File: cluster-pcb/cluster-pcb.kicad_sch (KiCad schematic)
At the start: 0 parts

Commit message: Progress toward v2.0
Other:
- sheet microcontroller ports: added none; removed ENABLE_TXRX_0, ENABLE_TXRX_1, ENABLE_TXRX_2, ENABLE_TXRX_3, ENABLE_TXRX_4, ENABLE_TXRX_5, ENABLE_TXRX_6, MUX_ADDRESS_0, MUX_ADDRESS_1, MUX_ADDRESS_2, RX, TX
- sheet prism-0 ports: added CIPO, COPI, SCK, ~{CS}; removed none
- sheet prism-1 ports: added CIPO, COPI, SCK, ~{CS}; removed none
- sheet prism-2 ports: added CIPO, COPI, SCK, ~{CS}; removed none
- sheet prism-3 ports: added CIPO, COPI, SCK, ~{CS}; removed ENABLE_TXRX, RX, TX
- sheet prism-4 ports: added CIPO, COPI, SCK, ~{CS}; removed none
- sheet prism-5 ports: added CIPO, COPI, SCK, ~{CS}; removed none
- sheet prism-6 ports: added CIPO, COPI, SCK, ~{CS}; removed none

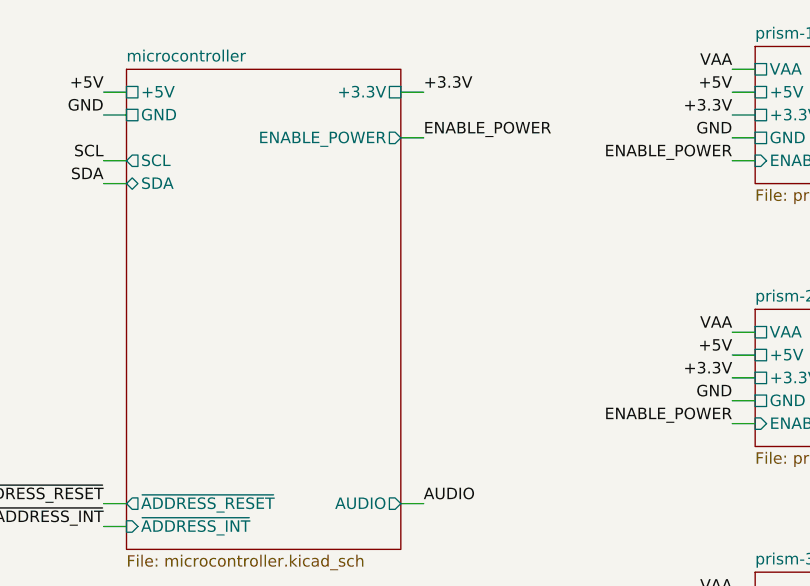
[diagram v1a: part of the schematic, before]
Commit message: Initial pcb layout
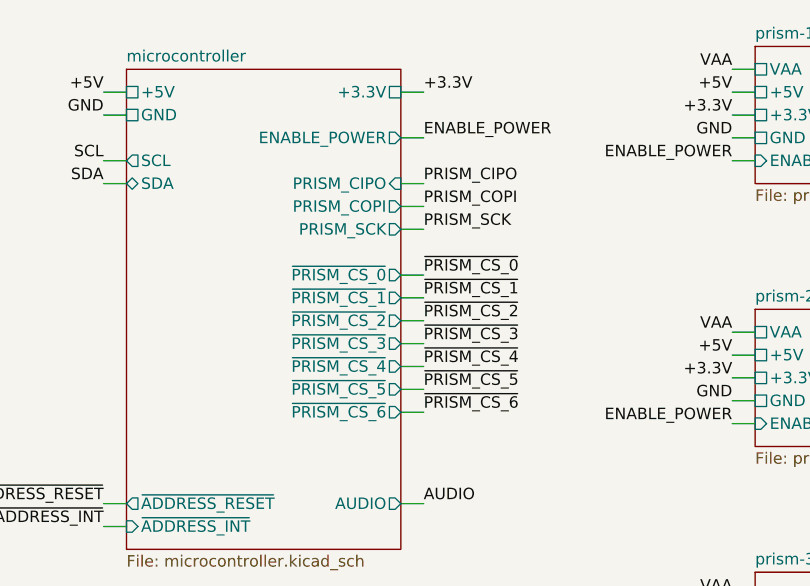
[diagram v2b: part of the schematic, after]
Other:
- sheet microcontroller ports: added PRISM_CIPO, PRISM_COPI, PRISM_SCK, ~{PRISM_CS_0}, ~{PRISM_CS_1}, ~{PRISM_CS_2}, ~{PRISM_CS_3}, ~{PRISM_CS_4}, ~{PRISM_CS_5}, ~{PRISM_CS_6}; removed none
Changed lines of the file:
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@@
   (title_block
     (title "cluster-pcb")
-    (date "2024-09-20")
+    (date "2024-09-27")
     (rev "2.0")
     (company "Howard Hughes Medical Institute")
   )
+  (wire (pts (xy 120.65 78.74) (xy 123.19 78.74))
+    (stroke (width 0) (type default))
+  )
+  (wire (pts (xy 120.65 88.9) (xy 123.19 88.9))
+    (stroke (width 0) (type default))
+  )
   (wire (pts (xy 242.57 41.91) (xy 245.11 41.91))
     (stroke (width 0) (type default))
   )
+  (wire (pts (xy 120.65 101.6) (xy 123.19 101.6))
+    (stroke (width 0) (type default))
+  )
   (wire (pts (xy 177.8 34.29) (xy 180.34 34.29))
     (stroke (width 0) (type default))
   )
+  (wire (pts (xy 120.65 99.06) (xy 123.19 99.06))
+    (stroke (width 0) (type default))
+  )
   (wire (pts (xy 177.8 39.37) (xy 180.34 39.37))
     (stroke (width 0) (type default))
@@
     (stroke (width 0) (type default))
   )
+  (wire (pts (xy 120.65 91.44) (xy 123.19 91.44))
+    (stroke (width 0) (type default))
+  )
   (wire (pts (xy 87.63 66.04) (xy 90.17 66.04))
     (stroke (width 0) (type default))
@@
     (stroke (width 0) (type default))
   )
+  (wire (pts (xy 120.65 86.36) (xy 123.19 86.36))
+    (stroke (width 0) (type default))
+  )
   (wire (pts (xy 222.25 34.29) (xy 224.79 34.29))
     (stroke (width 0) (type default))
@@
     (stroke (width 0) (type default))
   )
+  (wire (pts (xy 120.65 81.28) (xy 123.19 81.28))
+    (stroke (width 0) (type default))
+  )
   (wire (pts (xy 123.19 66.04) (xy 120.65 66.04))
     (stroke (width 0) (type default))
@@
     (stroke (width 0) (type default))
   )
+  (wire (pts (xy 120.65 93.98) (xy 123.19 93.98))
+    (stroke (width 0) (type default))
+  )
   (wire (pts (xy 120.65 71.12) (xy 123.19 71.12))
     (stroke (width 0) (type default))
@@
     (stroke (width 0) (type default))
   )
+  (wire (pts (xy 120.65 96.52) (xy 123.19 96.52))
+    (stroke (width 0) (type default))
+  )
   (wire (pts (xy 160.02 44.45) (xy 157.48 44.45))
     (stroke (width 0) (type default))
@@
     (stroke (width 0) (type default))
   )
+  (wire (pts (xy 120.65 76.2) (xy 123.19 76.2))
+    (stroke (width 0) (type default))
+  )
   (wire (pts (xy 222.25 97.79) (xy 224.79 97.79))
     (stroke (width 0) (type default))
@@
     (effects (font (size 1.27 1.27)) (justify left bottom))
   )
+  (label "~{PRISM_CS_4}" (at 123.19 96.52 0) (fields_autoplaced)
+    (effects (font (size 1.27 1.27)) (justify left bottom))
+  )
   (label "AUDIO" (at 123.19 111.76 0) (fields_autoplaced)
     (effects (font (size 1.27 1.27)) (justify left bottom))
@@
     (effects (font (size 1.27 1.27)) (justify right bottom))
   )
+  (label "PRISM_CIPO" (at 123.19 76.2 0) (fields_autoplaced)
+    (effects (font (size 1.27 1.27)) (justify left bottom))
+  )
   (label "PRISM_COPI" (at 245.11 95.25 0) (fields_autoplaced)
     (effects (font (size 1.27 1.27)) (justify left bottom))
@@
     (effects (font (size 1.27 1.27)) (justify right bottom))
   )
+  (label "~{PRISM_CS_6}" (at 123.19 101.6 0) (fields_autoplaced)
+    (effects (font (size 1.27 1.27)) (justify left bottom))
+  )
   (label "PRISM_CIPO" (at 180.34 92.71 0) (fields_autoplaced)
     (effects (font (size 1.27 1.27)) (justify left bottom))
   )
+  (label "~{PRISM_CS_1}" (at 123.19 88.9 0) (fields_autoplaced)
+    (effects (font (size 1.27 1.27)) (justify left bottom))
+  )
   (label "GND" (at 157.48 41.91 180) (fields_autoplaced)
     (effects (font (size 1.27 1.27)) (justify right bottom))
@@
     (effects (font (size 1.27 1.27)) (justify right bottom))
   )
+  (label "~{PRISM_CS_3}" (at 123.19 93.98 0) (fields_autoplaced)
+    (effects (font (size 1.27 1.27)) (justify left bottom))
+  )
   (label "+3.3V" (at 222.25 68.58 180) (fields_autoplaced)
     (effects (font (size 1.27 1.27)) (justify right bottom))
@@
     (effects (font (size 1.27 1.27)) (justify left bottom))
   )
+  (label "PRISM_SCK" (at 123.19 81.28 0) (fields_autoplaced)
+    (effects (font (size 1.27 1.27)) (justify left bottom))
+  )
   (label "PRISM_SCK" (at 245.11 68.58 0) (fields_autoplaced)
     (effects (font (size 1.27 1.27)) (justify left bottom))
@@
     (effects (font (size 1.27 1.27)) (justify right bottom))
   )
+  (label "~{PRISM_CS_5}" (at 123.19 99.06 0) (fields_autoplaced)
+    (effects (font (size 1.27 1.27)) (justify left bottom))
+  )
   (label "+3.3V" (at 157.48 97.79 180) (fields_autoplaced)
     (effects (font (size 1.27 1.27)) (justify right bottom))
@@
     (effects (font (size 1.27 1.27)) (justify left bottom))
   )
+  (label "~{PRISM_CS_2}" (at 123.19 91.44 0) (fields_autoplaced)
+    (effects (font (size 1.27 1.27)) (justify left bottom))
+  )
+  (label "PRISM_COPI" (at 123.19 78.74 0) (fields_autoplaced)
+    (effects (font (size 1.27 1.27)) (justify left bottom))
+  )
   (label "+5V" (at 222.25 66.04 180) (fields_autoplaced)
     (effects (font (size 1.27 1.27)) (justify right bottom))
+  )
+  (label "~{PRISM_CS_0}" (at 123.19 86.36 0) (fields_autoplaced)
+    (effects (font (size 1.27 1.27)) (justify left bottom))
   )
   (label "VAA" (at 222.25 63.5 180) (fields_autoplaced)
@@
       (effects (font (size 1.27 1.27)) (justify left))
     )
+    (pin "PRISM_COPI" output (at 120.65 78.74 0)
+      (effects (font (size 1.27 1.27)) (justify right))
+    )
+    (pin "PRISM_CIPO" input (at 120.65 76.2 0)
+      (effects (font (size 1.27 1.27)) (justify right))
+    )
+    (pin "~{PRISM_CS_0}" output (at 120.65 86.36 0)
+      (effects (font (size 1.27 1.27)) (justify right))
+    )
+    (pin "~{PRISM_CS_1}" output (at 120.65 88.9 0)
+      (effects (font (size 1.27 1.27)) (justify right))
+    )
+    (pin "PRISM_SCK" output (at 120.65 81.28 0)
+      (effects (font (size 1.27 1.27)) (justify right))
+    )
+    (pin "~{PRISM_CS_2}" output (at 120.65 91.44 0)
+      (effects (font (size 1.27 1.27)) (justify right))
+    )
+    (pin "~{PRISM_CS_3}" output (at 120.65 93.98 0)
+      (effects (font (size 1.27 1.27)) (justify right))
+    )
+    (pin "~{PRISM_CS_4}" output (at 120.65 96.52 0)
+      (effects (font (size 1.27 1.27)) (justify right))
+    )
+    (pin "~{PRISM_CS_5}" output (at 120.65 99.06 0)
+      (effects (font (size 1.27 1.27)) (justify right))
+    )
+    (pin "~{PRISM_CS_6}" output (at 120.65 101.6 0)
+      (effects (font (size 1.27 1.27)) (justify right))
+    )
     (instances
